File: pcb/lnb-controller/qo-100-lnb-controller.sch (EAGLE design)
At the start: 71 parts, among them CON1 2EDG-2P, Q1 AO3401, U1 LT8636, U2 ADP7142AUJZ-3.3, U3 DSC1201DE3-25M00000, U4 DSB321SDA, U5 MXT573ABC25M0000

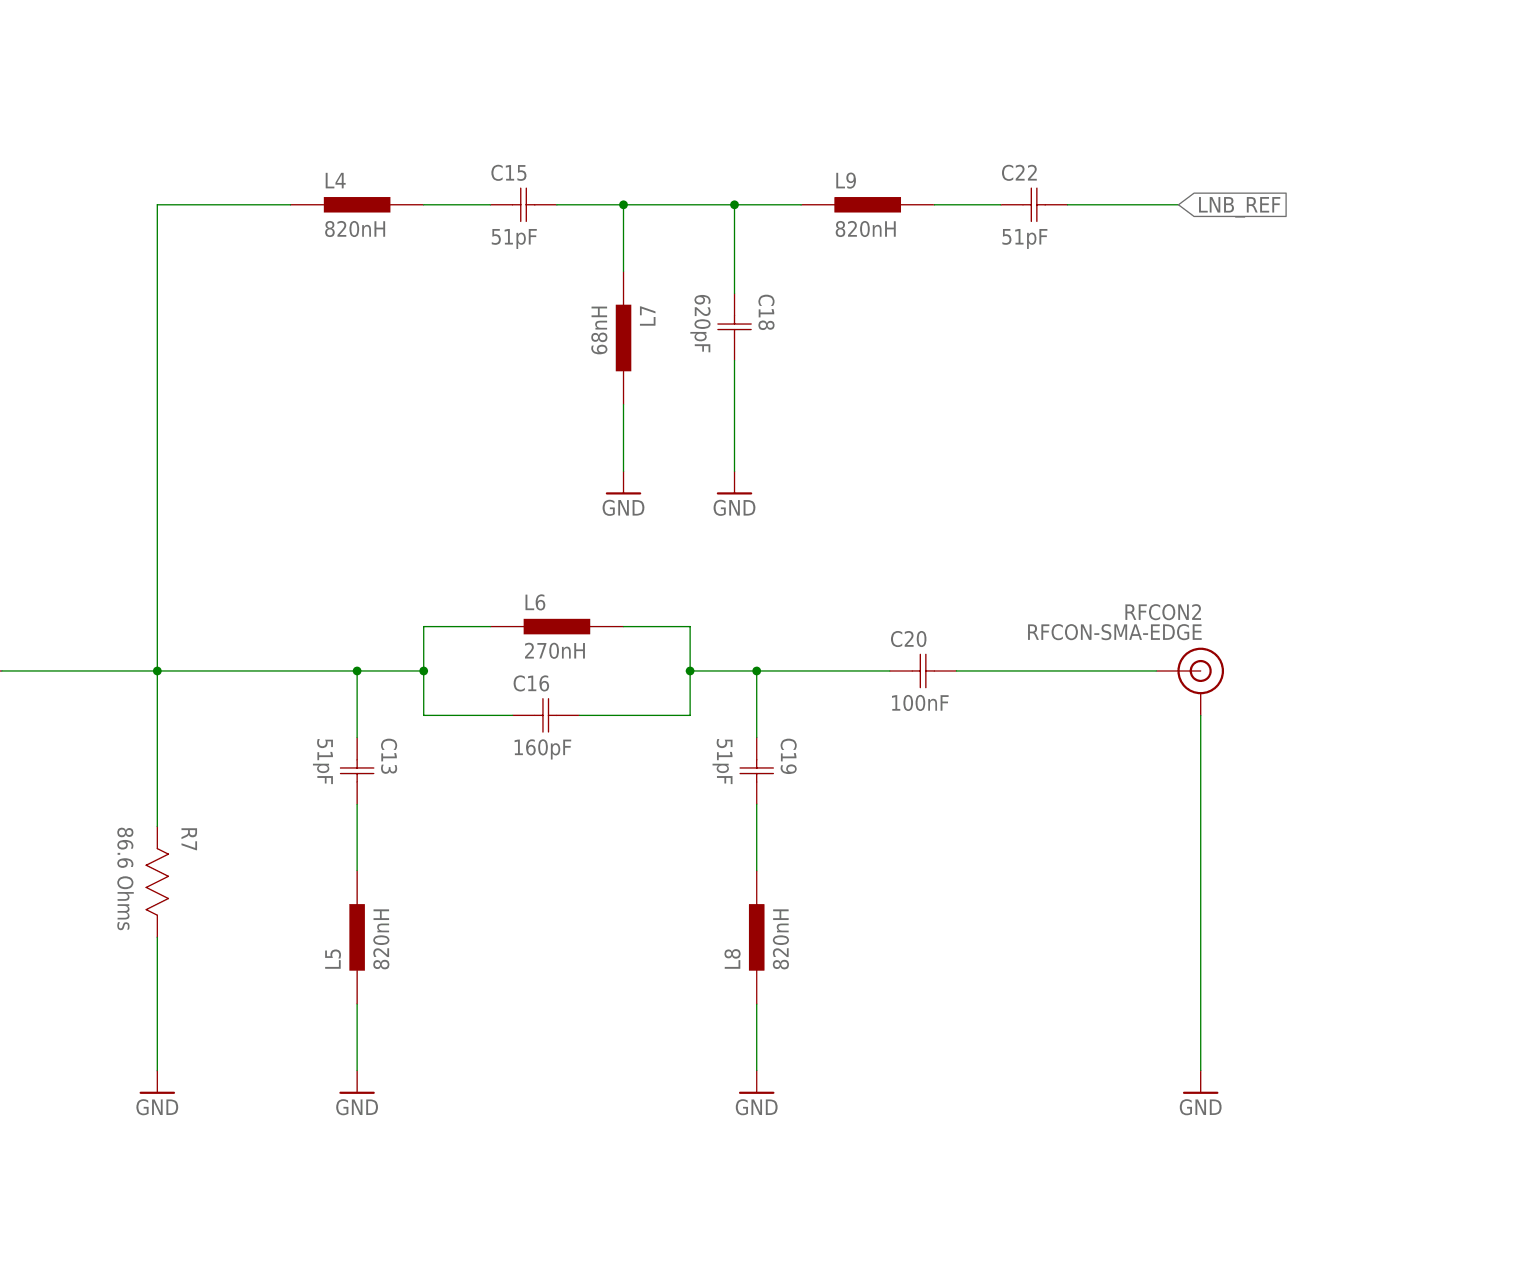
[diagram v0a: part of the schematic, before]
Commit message: GPSDO progress Added general filter PCB
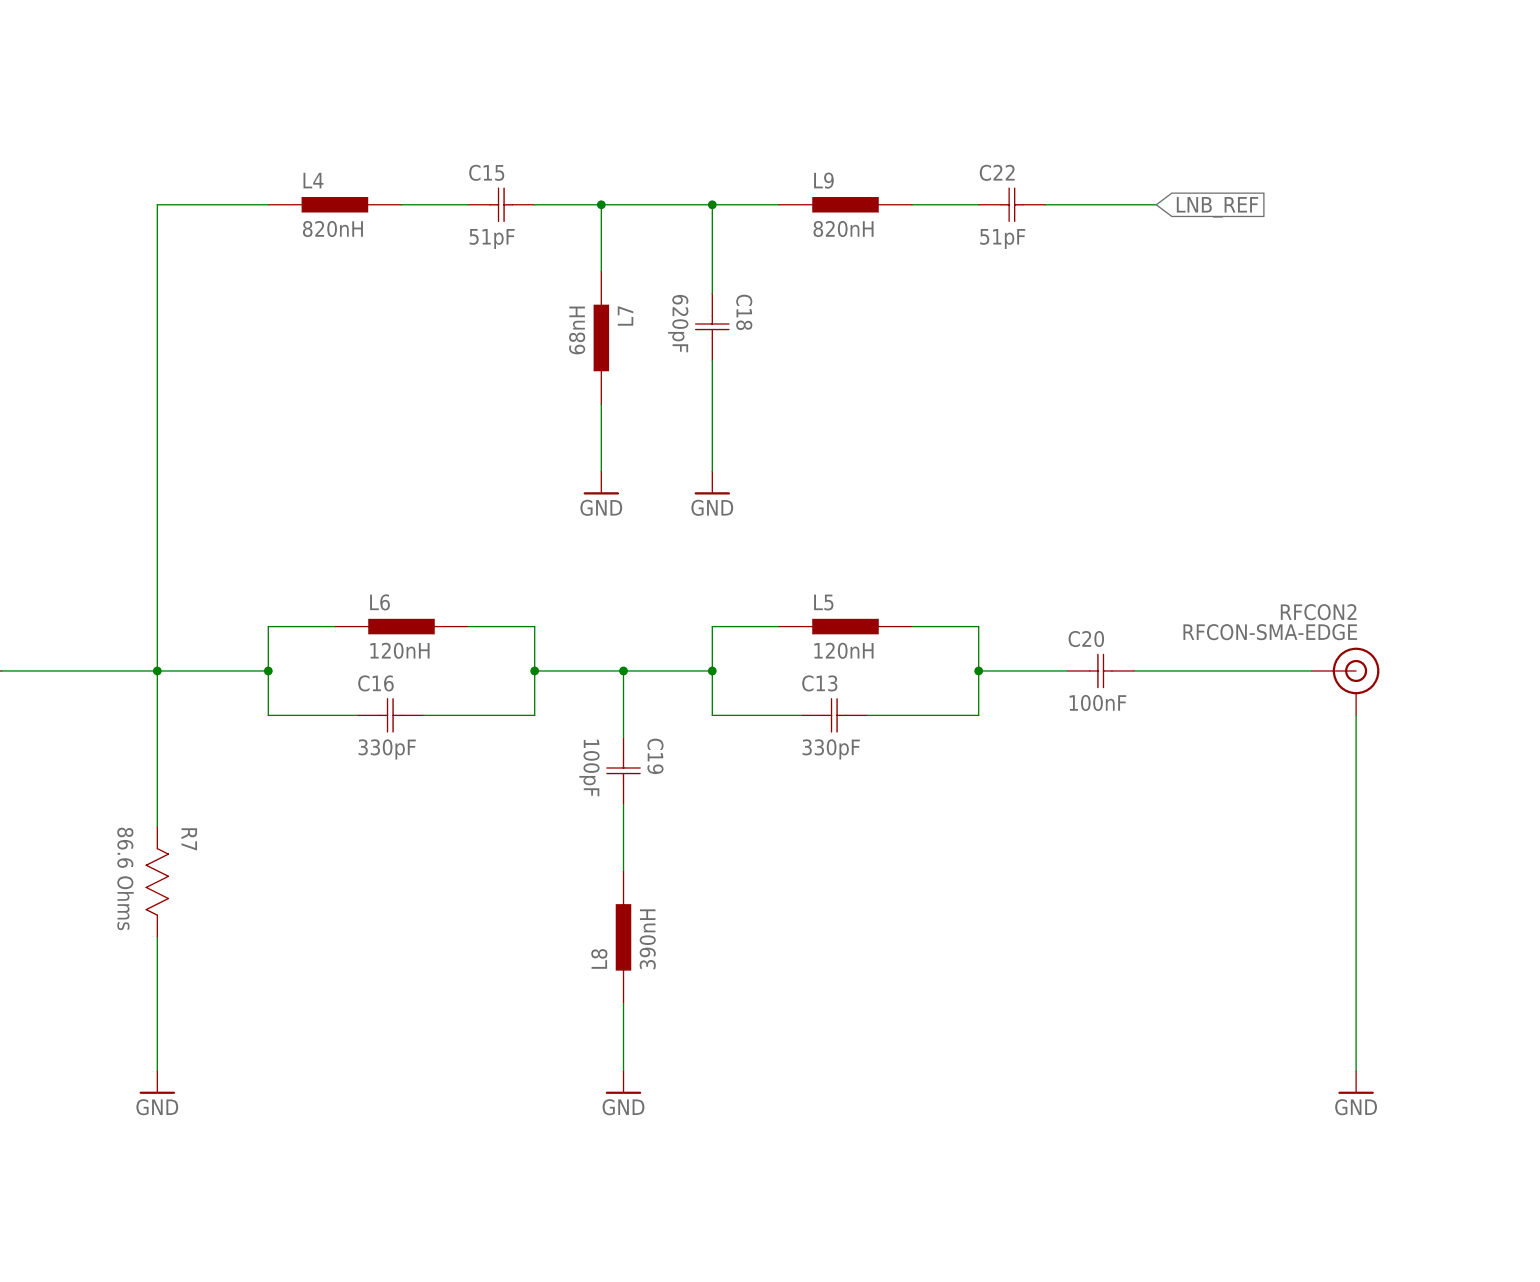
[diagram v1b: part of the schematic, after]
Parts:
- C13: value 51pF -> 330pF
- C16: value 160pF -> 330pF
- C19: value 51pF -> 100pF
- L5: value 820nH -> 120nH
- L6: value 270nH -> 120nH
- L8: value 820nH -> 390nH
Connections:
- net GND: no longer L5.1
- net N$16: now also C20.C1
- net N$17: no longer C13.C1
- net N$18: now also C13.C1, L5.1; no longer C20.C1
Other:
- moved on the sheet: C13, C15, C16, C18, C19, C20, C22, L4, L5, L6, L7, L8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

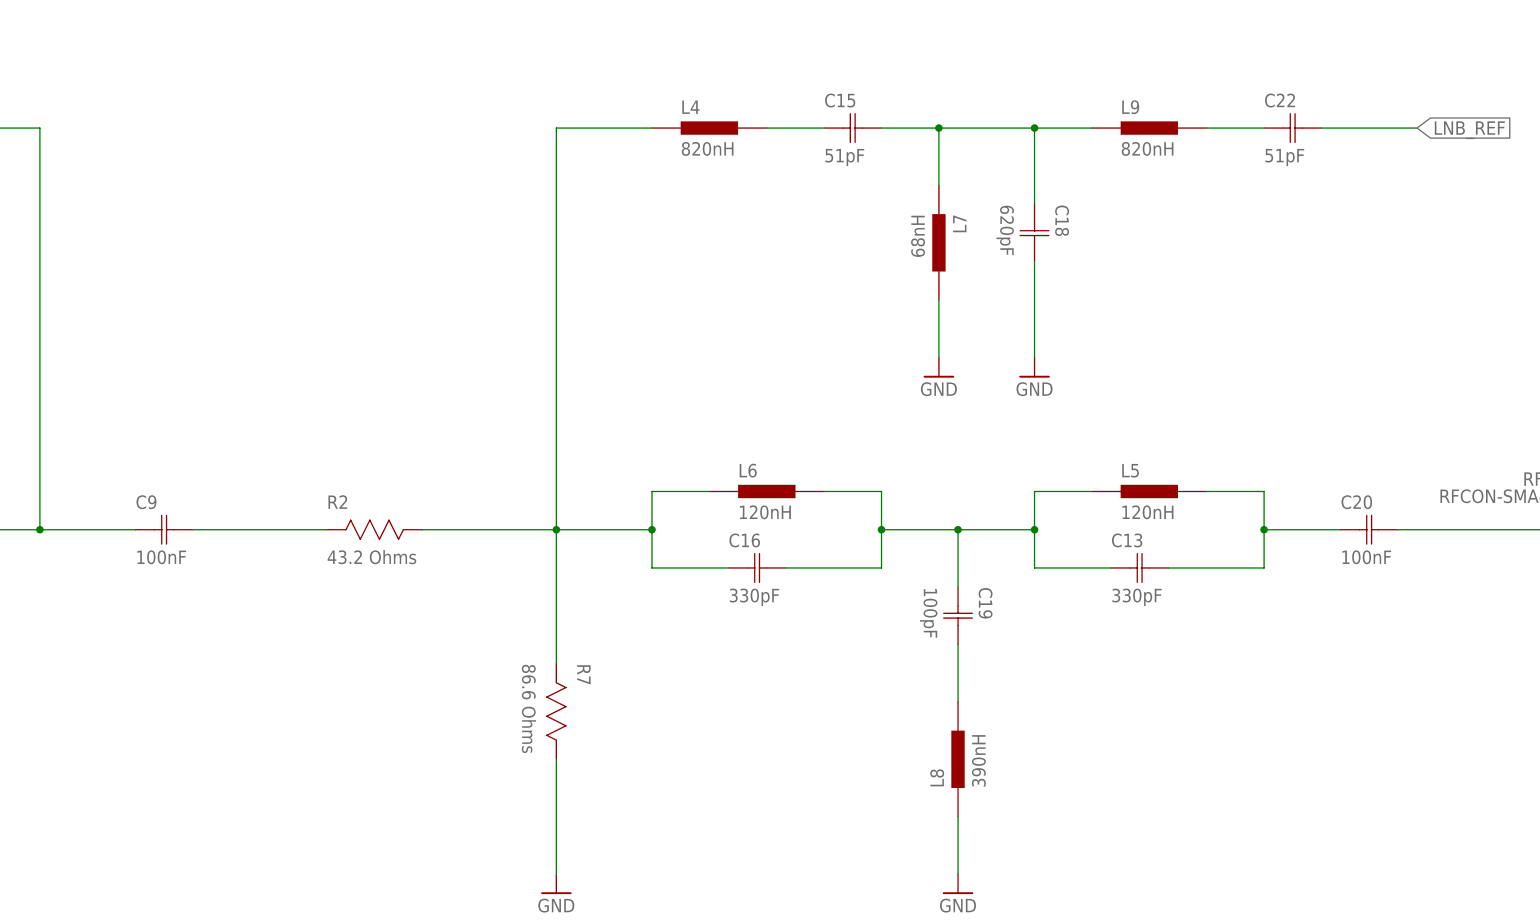
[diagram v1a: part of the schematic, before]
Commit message: Change some component values
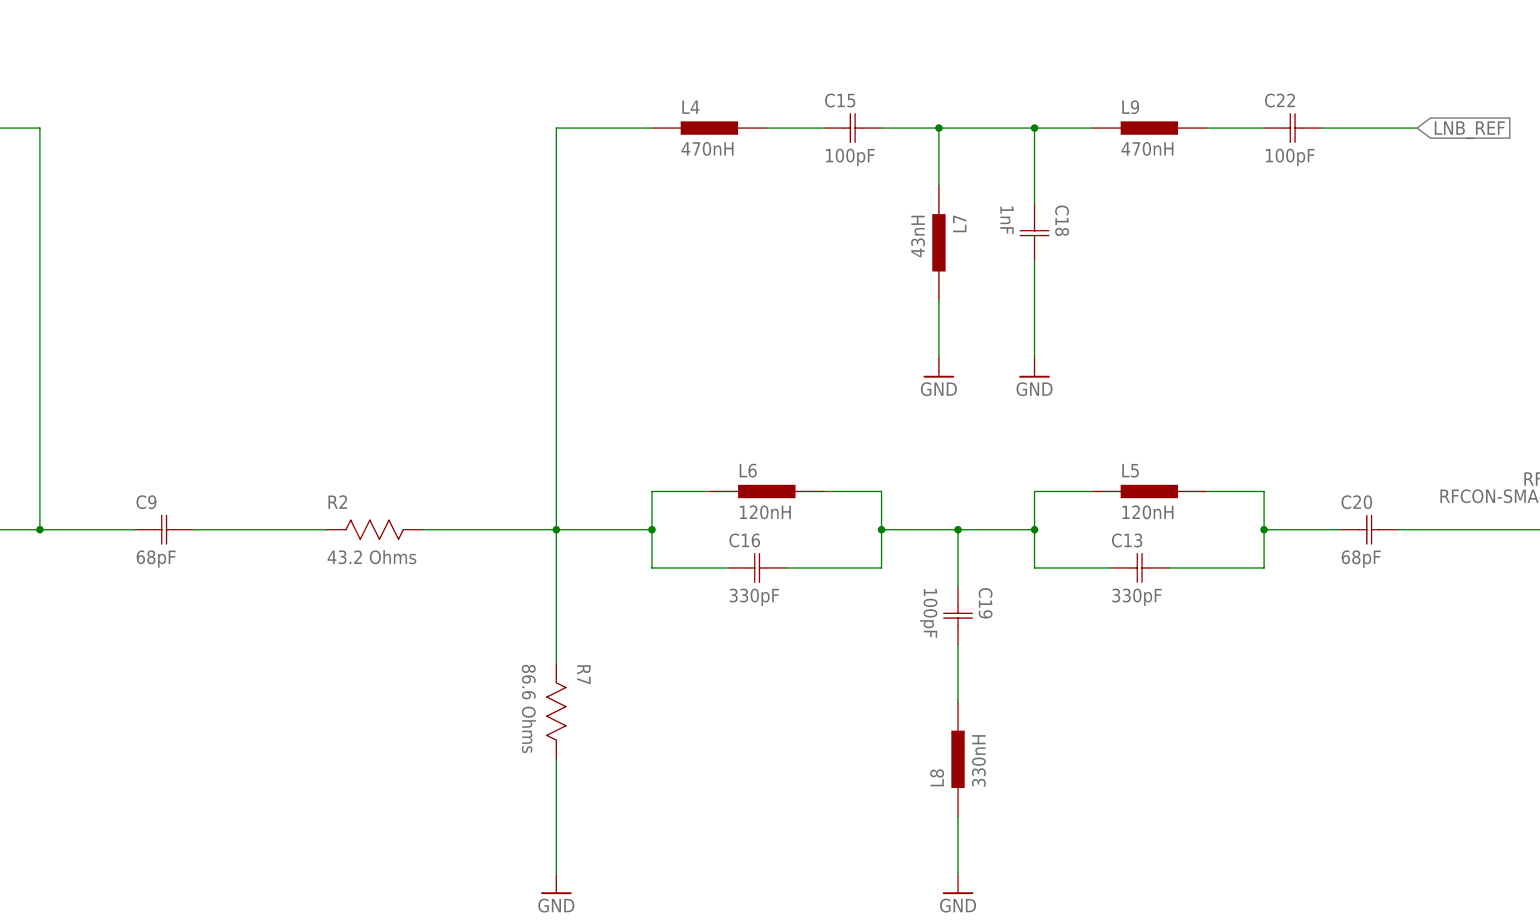
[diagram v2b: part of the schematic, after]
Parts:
- C15, C22: value 51pF -> 100pF
- C18: value 620pF -> 1nF
- C20, C9: value 100nF -> 68pF
- L4, L9: value 820nH -> 470nH
- L7: value 68nH -> 43nH
- L8: value 390nH -> 330nH
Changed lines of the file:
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@@
 <part name="R2" library="Resistor" deviceset="RESISTOR" device="-0603" value="43.2 Ohms"/>
 <part name="R7" library="Resistor" deviceset="RESISTOR" device="-0603" value="86.6 Ohms"/>
-<part name="C9" library="Capacitor" deviceset="CAPACITOR" device="-0603" value="100nF"/>
+<part name="C9" library="Capacitor" deviceset="CAPACITOR" device="-0603" value="68pF"/>
 <part name="L1" library="Inductor" deviceset="INDUCTOR" device="-0603" value="470nH">
 <attribute name="CURRENT" value="600 mA"/>
@@
 <part name="C8" library="Capacitor" deviceset="CAPACITOR" device="-0603" value="100nF"/>
 <part name="GND21" library="Supply Symbol" deviceset="GND" device=""/>
-<part name="C22" library="Capacitor" deviceset="CAPACITOR" device="-0603" value="51pF"/>
-<part name="L9" library="Inductor" deviceset="INDUCTOR" device="-0603" value="820nH"/>
-<part name="C18" library="Capacitor" deviceset="CAPACITOR" device="-0603" value="620pF"/>
-<part name="L7" library="Inductor" deviceset="INDUCTOR" device="-0603" value="68nH"/>
-<part name="C15" library="Capacitor" deviceset="CAPACITOR" device="-0603" value="51pF"/>
-<part name="L4" library="Inductor" deviceset="INDUCTOR" device="-0603" value="820nH"/>
+<part name="C22" library="Capacitor" deviceset="CAPACITOR" device="-0603" value="100pF"/>
+<part name="L9" library="Inductor" deviceset="INDUCTOR" device="-0603" value="470nH"/>
+<part name="C18" library="Capacitor" deviceset="CAPACITOR" device="-0603" value="1nF"/>
+<part name="L7" library="Inductor" deviceset="INDUCTOR" device="-0603" value="43nH"/>
+<part name="C15" library="Capacitor" deviceset="CAPACITOR" device="-0603" value="100pF"/>
+<part name="L4" library="Inductor" deviceset="INDUCTOR" device="-0603" value="470nH"/>
 <part name="GND22" library="Supply Symbol" deviceset="GND" device=""/>
 <part name="GND23" library="Supply Symbol" deviceset="GND" device=""/>
@@
 <part name="L6" library="Inductor" deviceset="INDUCTOR" device="-0603" value="120nH"/>
 <part name="C16" library="Capacitor" deviceset="CAPACITOR" device="-0603" value="330pF"/>
-<part name="C20" library="Capacitor" deviceset="CAPACITOR" device="-0603" value="100nF"/>
+<part name="C20" library="Capacitor" deviceset="CAPACITOR" device="-0603" value="68pF"/>
 <part name="JP3" library="Pin Header" deviceset="PINHD-1X2" device="" package3d_urn="urn:adsk.eagle:package:22435/2"/>
 <part name="U5" library="Microchip" deviceset="MXT57*" device="" technology="3ABC25M0000"/>
 <part name="C19" library="Capacitor" deviceset="CAPACITOR" device="-0603" value="100pF"/>
-<part name="L8" library="Inductor" deviceset="INDUCTOR" device="-0603" value="390nH"/>
+<part name="L8" library="Inductor" deviceset="INDUCTOR" device="-0603" value="330nH"/>
 <part name="GND14" library="Supply Symbol" deviceset="GND" device=""/>
 <part name="R9" library="Resistor" deviceset="RESISTOR" device="-0603" value="2.5K Ohms"/>

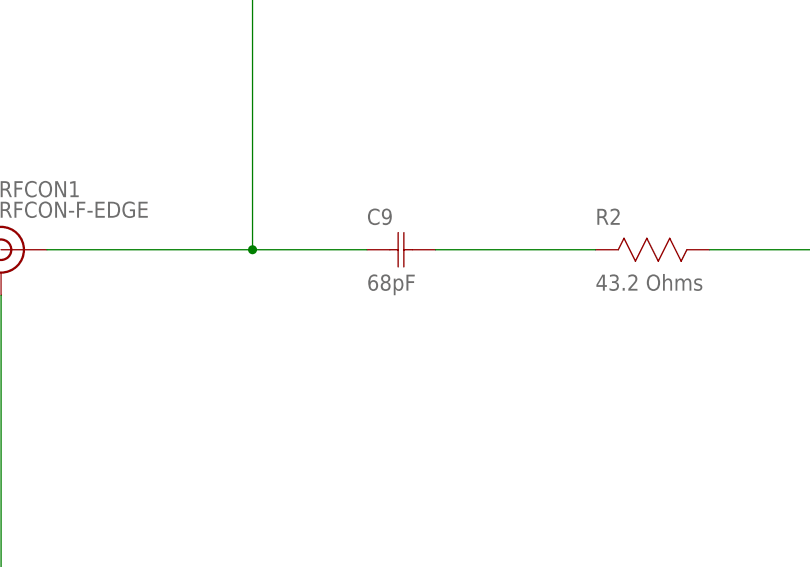
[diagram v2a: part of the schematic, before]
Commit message: Change upconverter input attenuation Rename general filter to generic filter Generate generic filter panel Change capacitor value on LNB controller Add PA gain response
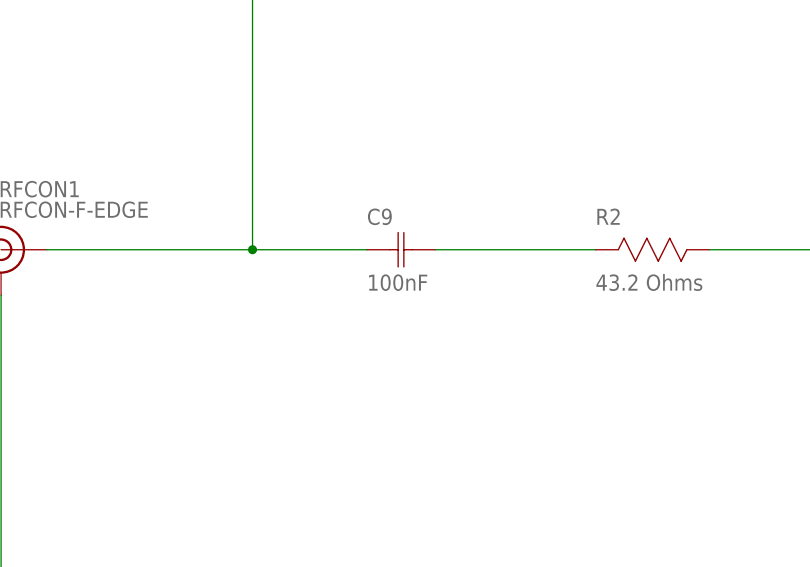
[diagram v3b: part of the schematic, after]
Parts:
- C9: value 68pF -> 100nF
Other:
- note added: "R2 & R7 form a 75 to 50 Ohm balun Install R2 = 0 Ohm and remove R7 if no impedance match is needed"
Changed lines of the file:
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@@
 <part name="R2" library="Resistor" deviceset="RESISTOR" device="-0603" value="43.2 Ohms"/>
 <part name="R7" library="Resistor" deviceset="RESISTOR" device="-0603" value="86.6 Ohms"/>
-<part name="C9" library="Capacitor" deviceset="CAPACITOR" device="-0603" value="68pF"/>
+<part name="C9" library="Capacitor" deviceset="CAPACITOR" device="-0603" value="100nF"/>
 <part name="L1" library="Inductor" deviceset="INDUCTOR" device="-0603" value="470nH">
 <attribute name="CURRENT" value="600 mA"/>
@@
 <text x="421.64" y="332.74" size="1.778" layer="98" rot="R90" align="center">VGSon = -6.5V at 13V
 VGSon = -9.0V at 18V</text>
+<text x="188.722" y="84.582" size="1.27" layer="98" rot="R180">R2 &amp; R7 form a 75 to 50 Ohm balun
+Install R2 = 0 Ohm and remove R7 if
+no impedance match is needed</text>
 </plain>
 <instances>
